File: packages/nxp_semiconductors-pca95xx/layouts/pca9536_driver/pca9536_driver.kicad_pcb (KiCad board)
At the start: 2 copper layers, 1 part

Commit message: WIP update pca95xx
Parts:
- C1: footprint atopile:C0402-b3ef17 -> Samsung_Electro_Mechanics_CL05B104KO5NNNC:C0402
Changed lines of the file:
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@@
     (net 1 "gnd")
     (net 2 "vdd")
-    (footprint "atopile:C0402-b3ef17"
+    (footprint "Samsung_Electro_Mechanics_CL05B104KO5NNNC:C0402"
         (layer "F.Cu")
         (at 0 0 0)
@@
                     (thickness 0.15)
                 )
-                (hide yes)
             )
         )
@@
             )
         )
-        (property "__atopile_lib_fp_hash__" "6c55d4e9-be4b-9c87-44df-b8e916bcf416"
+        (property "__atopile_lib_fp_hash__" "69b81097-78df-ad77-217e-5e8631ee5533"
             (at 0 0 0)
             (layer "User.9")
@@
         )
         (property "atopile_address" "decoupling_capacitor"
+            (at 0 0 0)
+            (layer "User.9")
+            (hide yes)
+            (effects
+                (font
+                    (size 0.125 0.125)
+                    (thickness 0.01875)
+                )
+            )
+        )
+        (property "checksum" "48f404f4744fe08fd1ebfc8a8a9fcd4da1e123065eb8fd6900bc8485463f45d5"
+            (at 0 0 0)
+            (layer "User.9")
+            (hide no)
+            (effects
+                (font
+                    (size 0.125 0.125)
+                    (thickness 0.01875)
+                )
+                (hide yes)
+            )
+        )
+        (property "Datasheet" "https://www.lcsc.com/datasheet/lcsc_datasheet_2304140030_Samsung-Electro-Mechanics-CL05B104KO5NNNC_C1525.pdf"
             (at 0 0 0)
             (layer "User.9")
@@
             (net 2 "vdd")
         )
+        (model "${KIPRJMOD}/../../parts/Samsung_Electro_Mechanics_CL05B104KO5NNNC/C0402_L1.0-W0.5-H0.5.step"
+            (offset
+                (xyz 0 0 0)
+            )
+            (scale
+                (xyz 1 1 1)
+            )
+            (rotate
+                (xyz 0 0 0)
+            )
+        )
     )

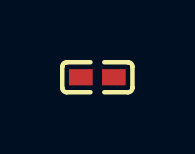
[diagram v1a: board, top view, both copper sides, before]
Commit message: Update 3D model locations
fix missing renders
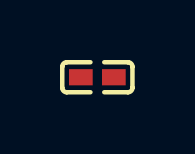
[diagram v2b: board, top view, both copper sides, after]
